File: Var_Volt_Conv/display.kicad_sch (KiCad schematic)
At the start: 9 parts, among them U301 NHD-C12832A1Z-FSW-FBW-3V3

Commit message: Add footprints for all capacitors, and record cap part names
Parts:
- C301, C302, C303, C304, C305, C306, C307, C308: footprint (none) -> Capacitor_SMD:C_0603_1608Metric
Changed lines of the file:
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@@
 			)
 		)
-		(property "Footprint" ""
+		(property "Footprint" "Capacitor_SMD:C_0603_1608Metric"
 			(at 182.5752 82.55 0)
 			(effects
@@
 			)
 		)
-		(property "Footprint" ""
+		(property "Footprint" "Capacitor_SMD:C_0603_1608Metric"
 			(at 157.1752 82.55 0)
 			(effects
@@
 			)
 		)
-		(property "Footprint" ""
+		(property "Footprint" "Capacitor_SMD:C_0603_1608Metric"
 			(at 169.8752 82.55 0)
 			(effects
@@
 			)
 		)
-		(property "Footprint" ""
+		(property "Footprint" "Capacitor_SMD:C_0603_1608Metric"
 			(at 178.7652 118.11 0)
 			(effects
@@
 			)
 		)
-		(property "Footprint" ""
+		(property "Footprint" "Capacitor_SMD:C_0603_1608Metric"
 			(at 163.5252 82.55 0)
 			(effects
@@
 			)
 		)
-		(property "Footprint" ""
+		(property "Footprint" "Capacitor_SMD:C_0603_1608Metric"
 			(at 176.2252 82.55 0)
 			(effects
@@
 			)
 		)
-		(property "Footprint" ""
+		(property "Footprint" "Capacitor_SMD:C_0603_1608Metric"
 			(at 178.7652 106.68 0)
 			(effects
@@
 			)
 		)
-		(property "Footprint" ""
+		(property "Footprint" "Capacitor_SMD:C_0603_1608Metric"
 			(at 148.2852 81.28 0)
 			(effects

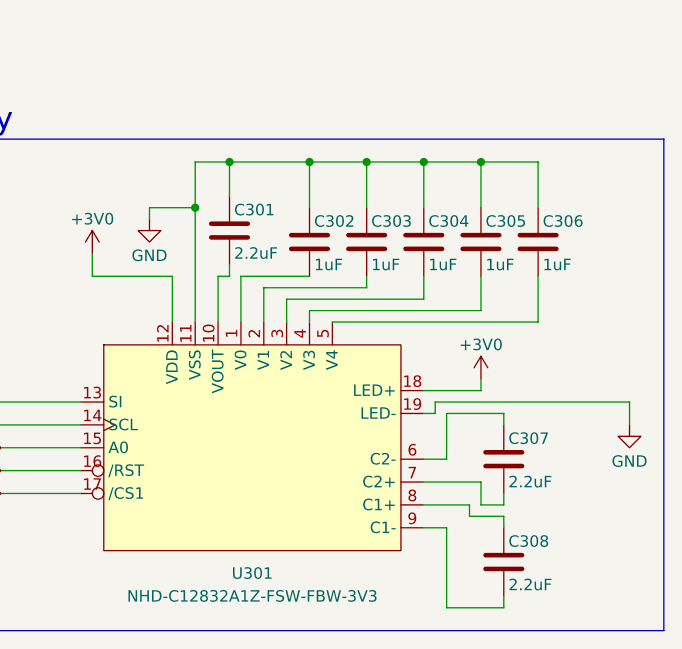
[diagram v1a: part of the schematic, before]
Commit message: Completed rough layout
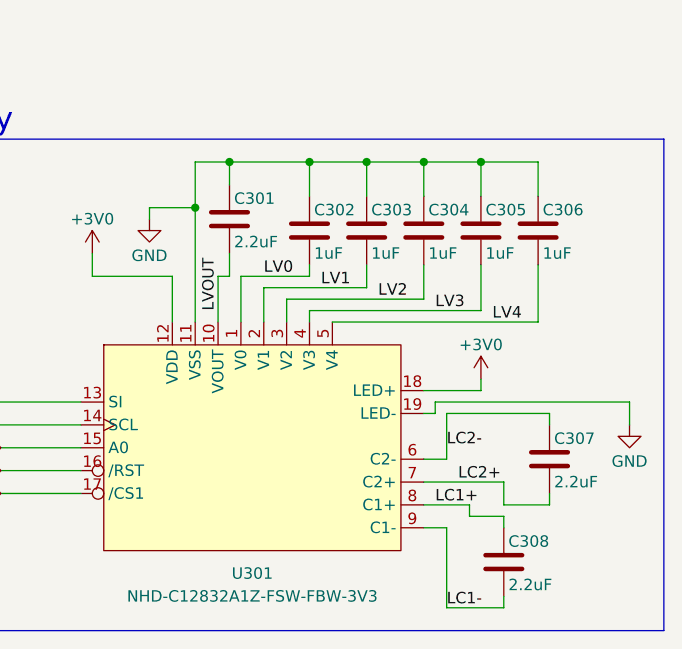
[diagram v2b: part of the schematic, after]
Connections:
- net LV4: now reaches C306.2, U301.5 (V4)
- net LV0: now reaches C302.2, U301.1 (V0)
- net LV2: now reaches C304.2, U301.3 (V2)
- net LC1+: now reaches C308.1, U301.8 (C1+)
- net LC1-: now reaches C308.2, U301.9 (C1-)
- net LVOUT: now reaches C301.2, U301.10 (VOUT)
- net LV1: now reaches C303.2, U301.2 (V1)
- net LV3: now reaches C305.2, U301.4 (V3)
- net LC2-: now reaches C307.1, U301.6 (C2-)
- net LC2+: now reaches C307.2, U301.7 (C2+)
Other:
- moved on the sheet: C301, C302, C303, C304, C305, C306, C307

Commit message: Routed signal traces and made power pours for microcontroller and display, also changed 4.7, 1uF and 2.2uF caps to 0402
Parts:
- C301, C302, C303, C304, C305, C306, C307, C308: footprint Capacitor_SMD:C_0603_1608Metric -> Capacitor_SMD:C_0402_1005Metric
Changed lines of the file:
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@@
 			)
 		)
-		(property "Footprint" "Capacitor_SMD:C_0603_1608Metric"
+		(property "Footprint" "Capacitor_SMD:C_0402_1005Metric"
 			(at 182.5752 81.28 0)
 			(effects
@@
 			)
 		)
-		(property "Footprint" "Capacitor_SMD:C_0603_1608Metric"
+		(property "Footprint" "Capacitor_SMD:C_0402_1005Metric"
 			(at 157.1752 81.28 0)
 			(effects
@@
 			)
 		)
-		(property "Footprint" "Capacitor_SMD:C_0603_1608Metric"
+		(property "Footprint" "Capacitor_SMD:C_0402_1005Metric"
 			(at 169.8752 81.28 0)
 			(effects
@@
 			)
 		)
-		(property "Footprint" "Capacitor_SMD:C_0603_1608Metric"
+		(property "Footprint" "Capacitor_SMD:C_0402_1005Metric"
 			(at 178.7652 118.11 0)
 			(effects
@@
 			)
 		)
-		(property "Footprint" "Capacitor_SMD:C_0603_1608Metric"
+		(property "Footprint" "Capacitor_SMD:C_0402_1005Metric"
 			(at 163.5252 81.28 0)
 			(effects
@@
 			)
 		)
-		(property "Footprint" "Capacitor_SMD:C_0603_1608Metric"
+		(property "Footprint" "Capacitor_SMD:C_0402_1005Metric"
 			(at 176.2252 81.28 0)
 			(effects
@@
 			)
 		)
-		(property "Footprint" "Capacitor_SMD:C_0603_1608Metric"
+		(property "Footprint" "Capacitor_SMD:C_0402_1005Metric"
 			(at 183.8452 106.68 0)
 			(effects
@@
 			)
 		)
-		(property "Footprint" "Capacitor_SMD:C_0603_1608Metric"
+		(property "Footprint" "Capacitor_SMD:C_0402_1005Metric"
 			(at 148.2852 80.01 0)
 			(effects

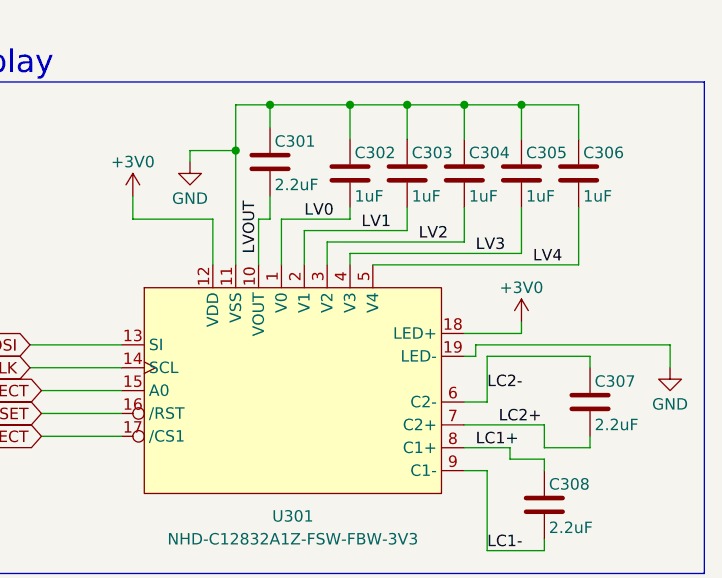
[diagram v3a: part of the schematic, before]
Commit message: Add Power, digital and analog grounds
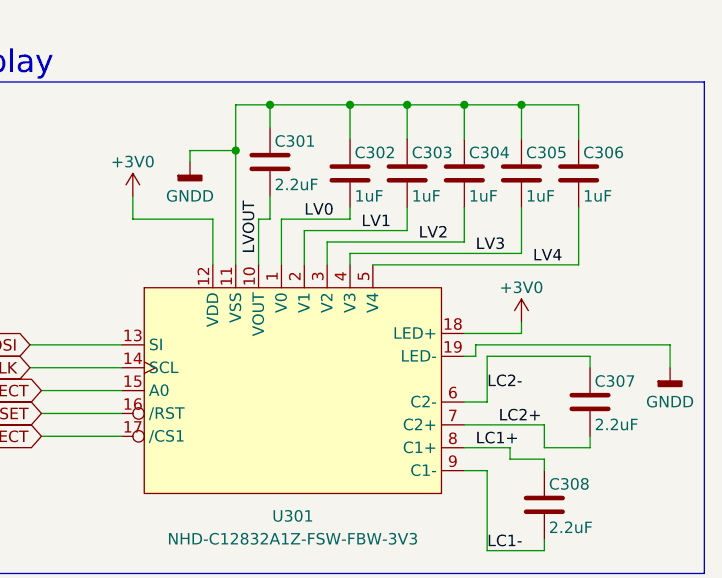
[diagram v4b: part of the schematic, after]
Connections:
- net GND renamed GNDD

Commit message: Labeled subcircuits in PCB
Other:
- title: (none) -> Variable Voltage Controller
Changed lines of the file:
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@@
 	(generator_version "8.0")
 	(paper "A4")
+	(title_block
+		(title "Variable Voltage Controller")
+		(date "2025-02-02")
+		(rev "1.0")
+	)
 	(junction
 		(at 175.26 69.85)

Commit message: Completed the BOM
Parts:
- C301, C307, C308: JLCPCB Part # (none) -> C72203; Manufacturer Part # (none) -> GRM155R61E225ME15D
- C302, C303, C304, C305, C306: JLCPCB Part # (none) -> C14445; Manufacturer Part # (none) -> CL05A105KP5NNNC
- U301: Manufacturer Part # (none) -> NHD-C12832A1Z-FSW-FBW-3V3
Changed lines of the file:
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@@
+			)
+		)
+		(property "JLCPCB Part #" "C14445"
+			(at 181.61 77.47 0)
+			(effects
+				(font
+					(size 1.27 1.27)
+				)
+				(hide yes)
+			)
+		)
+		(property "Manufacturer Part #" "CL05A105KP5NNNC"
+			(at 181.61 77.47 0)
+			(effects
+				(font
+					(size 1.27 1.27)
+				)
+				(hide yes)
 			)
 		)
@@
 			)
 		)
+		(property "JLCPCB Part #" "C14445"
+			(at 156.21 77.47 0)
+			(effects
+				(font
+					(size 1.27 1.27)
+				)
+				(hide yes)
+			)
+		)
+		(property "Manufacturer Part #" "CL05A105KP5NNNC"
+			(at 156.21 77.47 0)
+			(effects
+				(font
+					(size 1.27 1.27)
+				)
+				(hide yes)
+			)
+		)
 		(pin "2"
 		)
@@
 			)
 		)
+		(property "JLCPCB Part #" "C14445"
+			(at 168.91 77.47 0)
+			(effects
+				(font
+					(size 1.27 1.27)
+				)
+				(hide yes)
+			)
+		)
+		(property "Manufacturer Part #" "CL05A105KP5NNNC"
+			(at 168.91 77.47 0)
+			(effects
+				(font
+					(size 1.27 1.27)
+				)
+				(hide yes)
+			)
+		)
 		(pin "2"
 		)
@@
 		)
 		(property "Description" "Unpolarized capacitor"
+			(at 177.8 114.3 0)
+			(effects
+				(font
+					(size 1.27 1.27)
+				)
+				(hide yes)
+			)
+		)
+		(property "JLCPCB Part #" "C72203"
+			(at 177.8 114.3 0)
+			(effects
+				(font
+					(size 1.27 1.27)
+				)
+				(hide yes)
+			)
+		)
+		(property "Manufacturer Part #" "GRM155R61E225ME15D"
 			(at 177.8 114.3 0)
 			(effects
@@
 			)
 		)
+		(property "JLCPCB Part #" ""
+			(at 149.86 99.06 0)
+			(effects
+				(font
+					(size 1.27 1.27)
+				)
+				(hide yes)
+			)
+		)
+		(property "Manufacturer Part #" "NHD-C12832A1Z-FSW-FBW-3V3"
+			(at 149.86 99.06 0)
+			(effects
+				(font
+					(size 1.27 1.27)
+				)
+				(hide yes)
+			)
+		)
 		(pin "11"
 		)
@@
 			)
 		)
+		(property "JLCPCB Part #" "C14445"
+			(at 162.56 77.47 0)
+			(effects
+				(font
+					(size 1.27 1.27)
+				)
+				(hide yes)
+			)
+		)
+		(property "Manufacturer Part #" "CL05A105KP5NNNC"
+			(at 162.56 77.47 0)
+			(effects
+				(font
+					(size 1.27 1.27)
+				)
+				(hide yes)
+			)
+		)
 		(pin "2"
 		)
@@
 			)
 		)
+		(property "JLCPCB Part #" "C14445"
+			(at 175.26 77.47 0)
+			(effects
+				(font
+					(size 1.27 1.27)
+				)
+				(hide yes)
+			)
+		)
+		(property "Manufacturer Part #" "CL05A105KP5NNNC"
+			(at 175.26 77.47 0)
+			(effects
+				(font
+					(size 1.27 1.27)
+				)
+				(hide yes)
+			)
+		)
 		(pin "2"
 		)
@@
 			)
 		)
+		(property "JLCPCB Part #" "C72203"
+			(at 182.88 102.87 0)
+			(effects
+				(font
+					(size 1.27 1.27)
+				)
+				(hide yes)
+			)
+		)
+		(property "Manufacturer Part #" "GRM155R61E225ME15D"
+			(at 182.88 102.87 0)
+			(effects
+				(font
+					(size 1.27 1.27)
+				)
+				(hide yes)
+			)
+		)
 		(pin "2"
 		)
@@
 			(at 147.32 76.2 0)
 			(effects
+				(font
+					(size 1.27 1.27)
+				)
+				(hide yes)
+			)
+		)
+		(property "JLCPCB Part #" "C72203"
+			(at 147.32 76.2 0)
+			(effects
+				(font
+					(size 1.27 1.27)
+				)
+				(hide yes)
+			)
+		)
+		(property "Manufacturer Part #" "GRM155R61E225ME15D"
+			(at 147.32 76.2 0)
+			(effects

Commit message: Updated schematic, C121, R112 and SW201 now use components that are still in stock on JLCPCB
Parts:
- C301, C307, C308: JLCPCB Part # C72203 -> (none); LCSC (none) -> C72203
- C302, C303, C304, C305, C306: JLCPCB Part # C14445 -> (none); LCSC (none) -> C14445
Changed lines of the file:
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@@
-			)
-		)
-		(property "JLCPCB Part #" "C14445"
-			(at 181.61 77.47 0)
-			(effects
-				(font
-					(size 1.27 1.27)
-				)
-				(hide yes)
 			)
 		)
@@
 			)
 		)
+		(property "LCSC" "C14445"
+			(at 181.61 77.47 0)
+			(effects
+				(font
+					(size 1.27 1.27)
+				)
+				(hide yes)
+			)
+		)
 		(pin "2"
 		)
@@
 			)
 		)
-		(property "JLCPCB Part #" "C14445"
-			(at 156.21 77.47 0)
-			(effects
-				(font
-					(size 1.27 1.27)
-				)
-				(hide yes)
-			)
-		)
 		(property "Manufacturer Part #" "CL05A105KP5NNNC"
 			(at 156.21 77.47 0)
@@
 			)
 		)
+		(property "LCSC" "C14445"
+			(at 156.21 77.47 0)
+			(effects
+				(font
+					(size 1.27 1.27)
+				)
+				(hide yes)
+			)
+		)
 		(pin "2"
 		)
@@
 			)
 		)
-		(property "JLCPCB Part #" "C14445"
-			(at 168.91 77.47 0)
-			(effects
-				(font
-					(size 1.27 1.27)
-				)
-				(hide yes)
-			)
-		)
 		(property "Manufacturer Part #" "CL05A105KP5NNNC"
 			(at 168.91 77.47 0)
@@
 			)
 		)
+		(property "LCSC" "C14445"
+			(at 168.91 77.47 0)
+			(effects
+				(font
+					(size 1.27 1.27)
+				)
+				(hide yes)
+			)
+		)
 		(pin "2"
 		)
@@
 			)
 		)
-		(property "JLCPCB Part #" "C72203"
+		(property "Manufacturer Part #" "GRM155R61E225ME15D"
 			(at 177.8 114.3 0)
 			(effects
@@
 			)
 		)
-		(property "Manufacturer Part #" "GRM155R61E225ME15D"
+		(property "LCSC" "C72203"
 			(at 177.8 114.3 0)
 			(effects
@@
 			)
 		)
-		(property "JLCPCB Part #" ""
-			(at 149.86 99.06 0)
-			(effects
-				(font
-					(size 1.27 1.27)
-				)
-				(hide yes)
-			)
-		)
 		(property "Manufacturer Part #" "NHD-C12832A1Z-FSW-FBW-3V3"
 			(at 149.86 99.06 0)
@@
 			)
 		)
-		(property "JLCPCB Part #" "C14445"
-			(at 162.56 77.47 0)
-			(effects
-				(font
-					(size 1.27 1.27)
-				)
-				(hide yes)
-			)
-		)
 		(property "Manufacturer Part #" "CL05A105KP5NNNC"
 			(at 162.56 77.47 0)
@@
 			)
 		)
+		(property "LCSC" "C14445"
+			(at 162.56 77.47 0)
+			(effects
+				(font
+					(size 1.27 1.27)
+				)
+				(hide yes)
+			)
+		)
 		(pin "2"
 		)
@@
 			)
 		)
-		(property "JLCPCB Part #" "C14445"
-			(at 175.26 77.47 0)
-			(effects
-				(font
-					(size 1.27 1.27)
-				)
-				(hide yes)
-			)
-		)
 		(property "Manufacturer Part #" "CL05A105KP5NNNC"
 			(at 175.26 77.47 0)
@@
 			)
 		)
+		(property "LCSC" "C14445"
+			(at 175.26 77.47 0)
+			(effects
+				(font
+					(size 1.27 1.27)
+				)
+				(hide yes)
+			)
+		)
 		(pin "2"
 		)
@@
 			)
 		)
-		(property "JLCPCB Part #" "C72203"
-			(at 182.88 102.87 0)
-			(effects
-				(font
-					(size 1.27 1.27)
-				)
-				(hide yes)
-			)
-		)
 		(property "Manufacturer Part #" "GRM155R61E225ME15D"
 			(at 182.88 102.87 0)
@@
 			)
 		)
+		(property "LCSC" "C72203"
+			(at 182.88 102.87 0)
+			(effects
+				(font
+					(size 1.27 1.27)
+				)
+				(hide yes)
+			)
+		)
 		(pin "2"
 		)
@@
 			)
 		)
-		(property "JLCPCB Part #" "C72203"
-			(at 147.32 76.2 0)
-			(effects
-				(font
-					(size 1.27 1.27)
-				)
-				(hide yes)
-			)
-		)
 		(property "Manufacturer Part #" "GRM155R61E225ME15D"
 			(at 147.32 76.2 0)
 			(effects
+				(font
+					(size 1.27 1.27)
+				)
+				(hide yes)
+			)
+		)
+		(property "LCSC" "C72203"
+			(at 147.32 76.2 0)
+			(effects

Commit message: Confirmed all basic components
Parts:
- C301, C307, C308: LCSC C72203 -> (none); Manufacturer Part # GRM155R61E225ME15D -> CL05A225MQ5NSNC; lcsc (none) -> C12530
- C302, C303, C304, C305, C306: LCSC C14445 -> (none); Manufacturer Part # CL05A105KP5NNNC -> CL05A105KA5NQNC; lcsc (none) -> C52923
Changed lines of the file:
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@@
 			)
 		)
-		(property "Manufacturer Part #" "CL05A105KP5NNNC"
+		(property "Manufacturer Part #" "CL05A105KA5NQNC"
 			(at 181.61 77.47 0)
 			(effects
@@
 			)
 		)
-		(property "LCSC" "C14445"
+		(property "lcsc" "C52923"
 			(at 181.61 77.47 0)
 			(effects
@@
 			)
 		)
-		(property "Manufacturer Part #" "CL05A105KP5NNNC"
+		(property "Manufacturer Part #" "CL05A105KA5NQNC"
 			(at 156.21 77.47 0)
 			(effects
@@
 			)
 		)
-		(property "LCSC" "C14445"
+		(property "lcsc" "C52923"
 			(at 156.21 77.47 0)
 			(effects
@@
 			)
 		)
-		(property "Manufacturer Part #" "CL05A105KP5NNNC"
+		(property "Manufacturer Part #" "CL05A105KA5NQNC"
 			(at 168.91 77.47 0)
 			(effects
@@
 			)
 		)
-		(property "LCSC" "C14445"
+		(property "lcsc" "C52923"
 			(at 168.91 77.47 0)
 			(effects
@@
 			)
 		)
-		(property "Manufacturer Part #" "GRM155R61E225ME15D"
+		(property "Manufacturer Part #" "CL05A225MQ5NSNC"
 			(at 177.8 114.3 0)
 			(effects
@@
 			)
 		)
-		(property "LCSC" "C72203"
+		(property "lcsc" "C12530"
 			(at 177.8 114.3 0)
 			(effects
@@
 			)
 		)
-		(property "Manufacturer Part #" "CL05A105KP5NNNC"
+		(property "Manufacturer Part #" "CL05A105KA5NQNC"
 			(at 162.56 77.47 0)
 			(effects
@@
 			)
 		)
-		(property "LCSC" "C14445"
+		(property "lcsc" "C52923"
 			(at 162.56 77.47 0)
 			(effects
@@
 			)
 		)
-		(property "Manufacturer Part #" "CL05A105KP5NNNC"
+		(property "Manufacturer Part #" "CL05A105KA5NQNC"
 			(at 175.26 77.47 0)
 			(effects
@@
 			)
 		)
-		(property "LCSC" "C14445"
+		(property "lcsc" "C52923"
 			(at 175.26 77.47 0)
 			(effects
@@
 			)
 		)
-		(property "Manufacturer Part #" "GRM155R61E225ME15D"
+		(property "Manufacturer Part #" "CL05A225MQ5NSNC"
 			(at 182.88 102.87 0)
 			(effects
@@
 			)
 		)
-		(property "LCSC" "C72203"
+		(property "lcsc" "C12530"
 			(at 182.88 102.87 0)
 			(effects
@@
 			)
 		)
-		(property "Manufacturer Part #" "GRM155R61E225ME15D"
+		(property "Manufacturer Part #" "CL05A225MQ5NSNC"
 			(at 147.32 76.2 0)
 			(effects
@@
 			)
 		)
-		(property "LCSC" "C72203"
+		(property "lcsc" "C12530"
 			(at 147.32 76.2 0)
 			(effects
